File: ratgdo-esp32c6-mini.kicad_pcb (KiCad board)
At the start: 2 copper layers, 29 parts, among them J1 USB_C_Receptacle_USB2.0_14P, J2 Screw_Terminal_01x03, Q1 2N7002, Q2 AO3400A, SW1 RESET, SW2 BOOTSEL, U1 USBLC6-2SC6, U2 ESP32-C6-MINI-1/U, U3 RS3236-3.3YF5

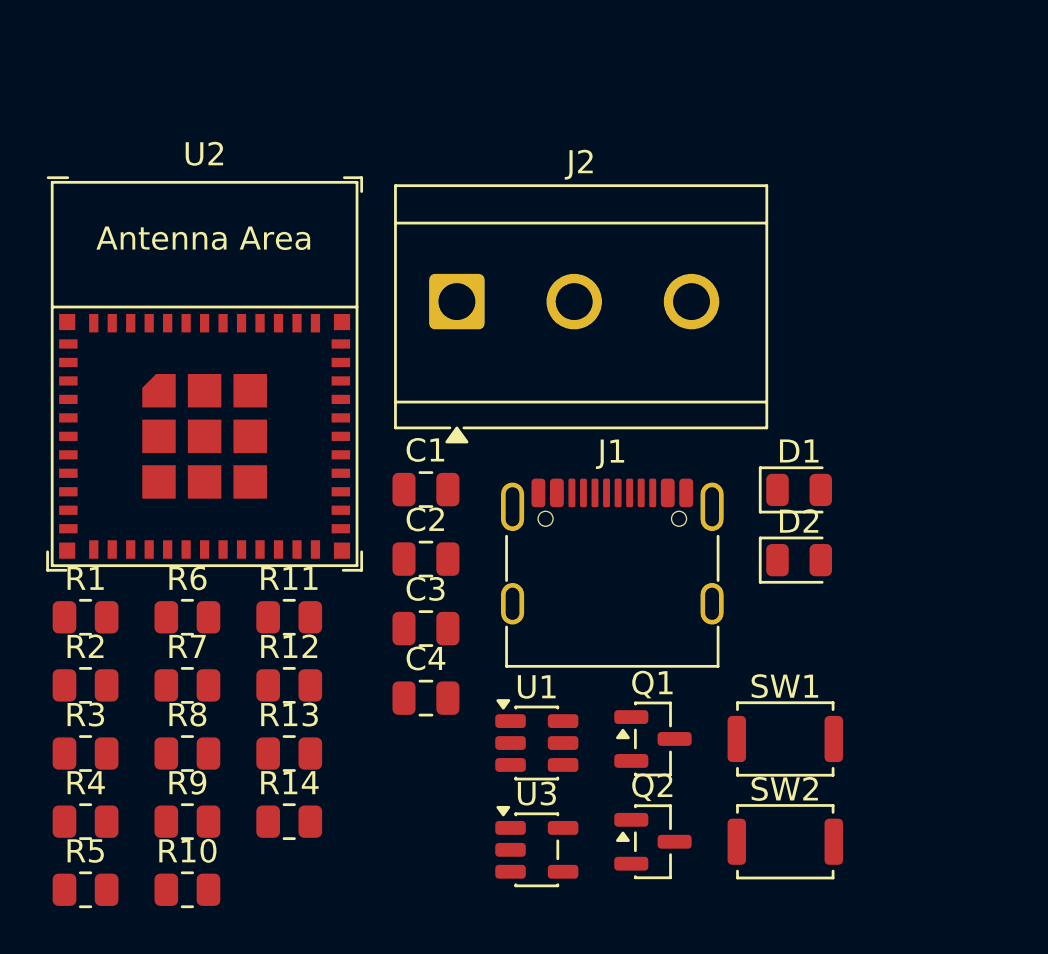
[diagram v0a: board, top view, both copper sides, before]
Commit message: change R&C to 0402 size
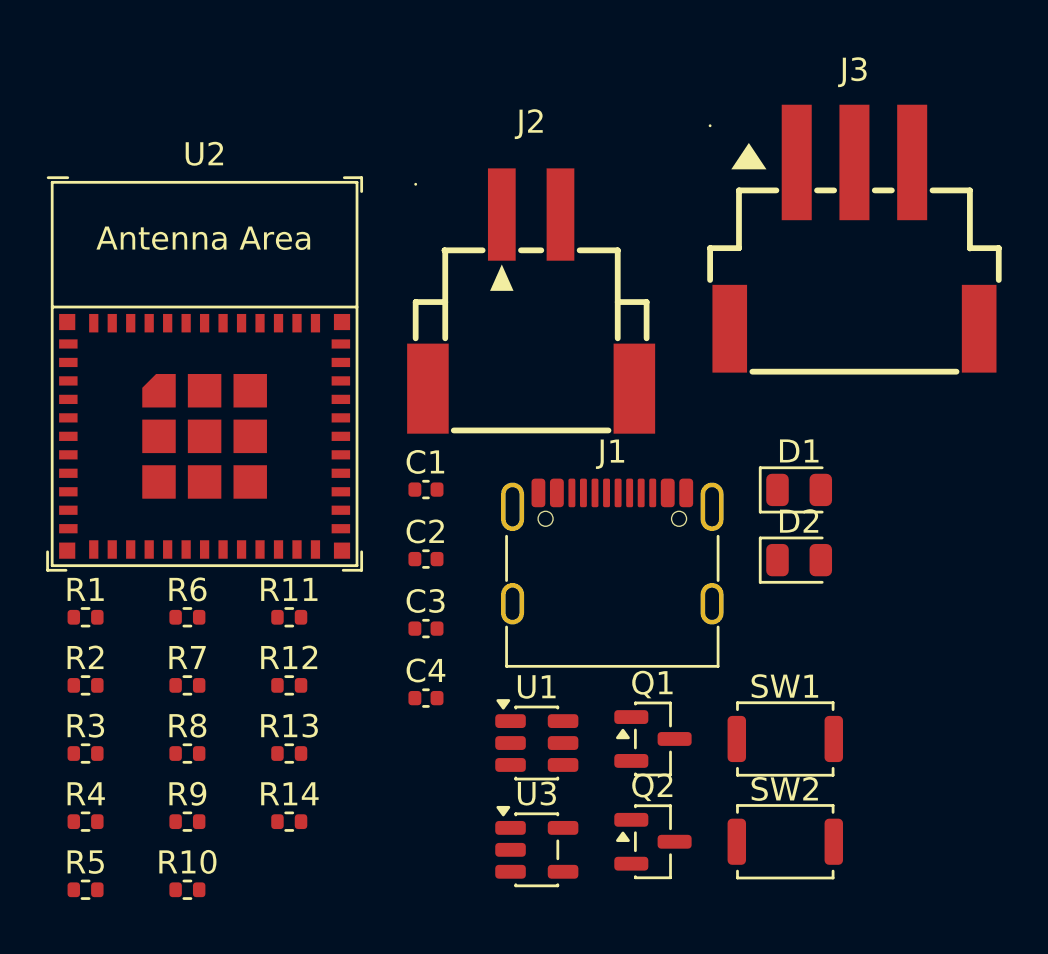
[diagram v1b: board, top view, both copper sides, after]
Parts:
- added J3: Conn_01x03, LCSC:CONN-SMD_3P-P2.50_HX-2.54-3P-WT, F.Cu at (63.5, 29.0)
- C1, C2, C3, C4: footprint Capacitor_SMD:C_0805_2012Metric -> Capacitor_SMD:C_0402_1005Metric
- J2: value Screw_Terminal_01x03 -> Conn_01x02; footprint TerminalBlock_CUI:TerminalBlock_CUI_TB007-508-03_1x03_P5.08mm_Horizontal -> LCSC:CONN-SMD_2P-P2.54-XH2.54-WT
- R1, R10, R11, R12, R13, R14, R2, R3, R4, R5, R6, R7, R8, R9: footprint Resistor_SMD:R_0805_2012Metric -> Resistor_SMD:R_0402_1005Metric
- moved J2 3.22 mm to (49.5, 31.4)
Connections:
- J2 pad 1: BLK/OBST -> +5V
- J2 pad 2: RED/CTRL -> GND
- J2 pad 3: GND -> (no net)

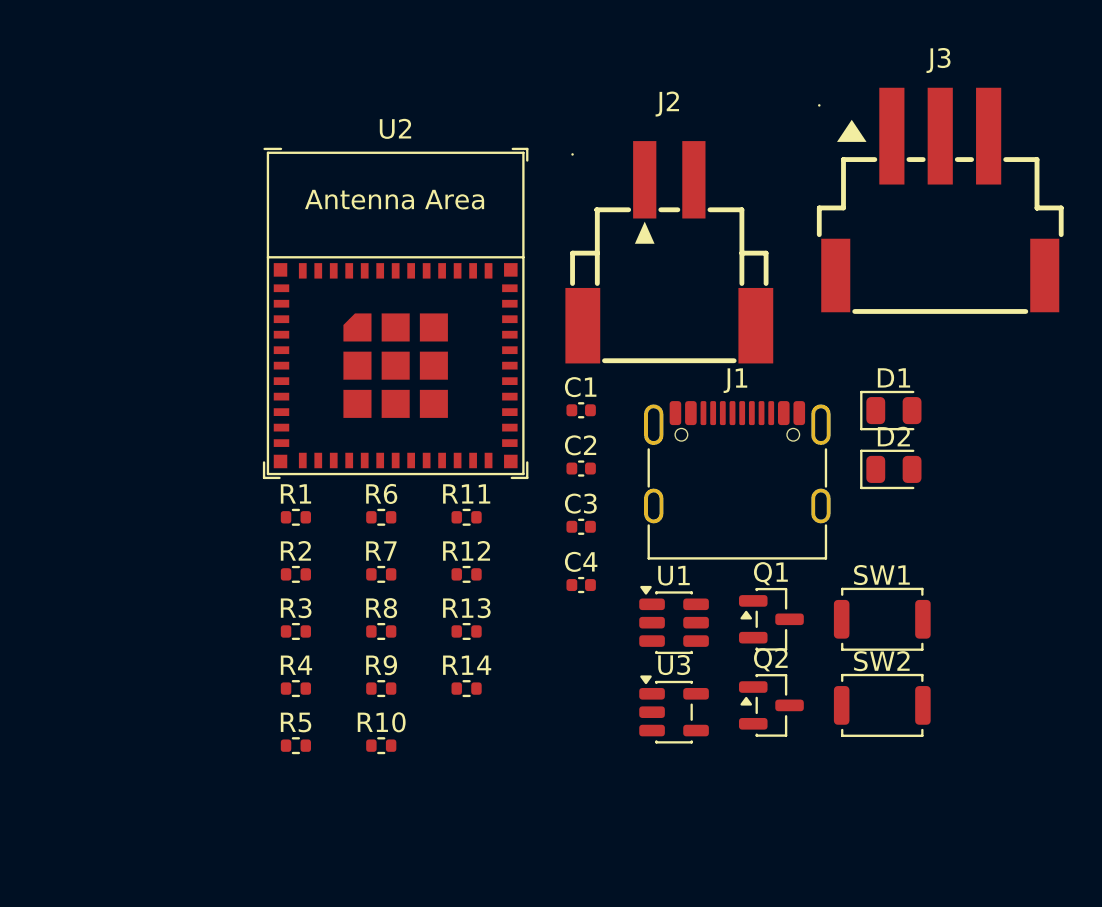
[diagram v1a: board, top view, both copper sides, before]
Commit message: sync pcb with schematic
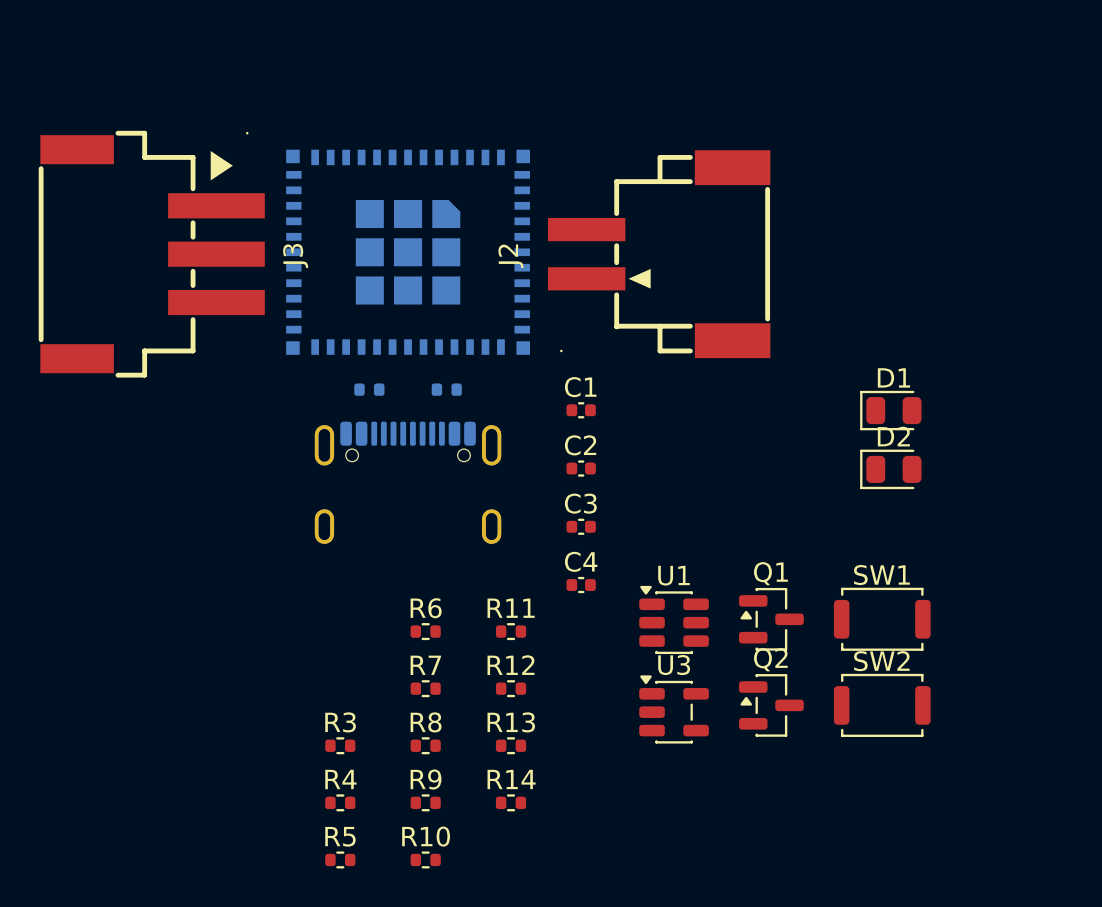
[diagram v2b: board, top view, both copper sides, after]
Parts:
- J1, R1, R2, U2: moved to B.Cu
- moved J3 41.1 mm to (22.5, 31.5), turned to -90 degrees
- moved J1 17.0 mm to (36.0, 44.5), turned to 180 degrees
- moved R2 10.3 mm to (34.0, 38.5), turned to 180 degrees
- moved R1 10.2 mm to (38.0, 38.5)
- moved R11 6.34 mm to (41.3, 51.0)
- moved R12 6.34 mm to (41.3, 54.0)
- moved R13 6.34 mm to (41.3, 56.9)
- moved R14 6.34 mm to (41.3, 59.9)
- moved R3 6.34 mm to (32.5, 56.9)
- moved R4 6.34 mm to (32.5, 59.9)
- moved R6 6.34 mm to (36.9, 51.0)
- moved R7 6.34 mm to (36.9, 54.0)
- moved R8 6.34 mm to (36.9, 56.9)
- moved R9 6.34 mm to (36.9, 59.9)
- moved R5 6.34 mm to (32.5, 62.8)
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
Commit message: layout components
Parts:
- J1: value USB_C_Receptacle_USB2.0_14P -> USB_C_2.0
- J2, J3: moved to B.Cu
- R1, R2: moved to F.Cu
- U2: value ESP32-C6-MINI-1/U -> ESP32-C6-MINI
- U3: value RS3236-3.3YF5 -> RS3236
- moved R1 139.8 mm to (161.0, 105.0)
- moved J2 139.4 mm to (171.0, 99.0), turned to -90 degrees
- moved J3 139.3 mm to (144.5, 98.8), turned to 90 degrees
- moved U2 138.3 mm to (158.0, 93.9)
- moved R2 138.1 mm to (155.0, 105.0)
- moved J1 137.9 mm to (158.0, 108.7)
- moved C1 135.1 mm to (166.0, 99.5), turned to -90 degrees
- moved R3 133.8 mm to (159.0, 100.5)
- moved R4 131.0 mm to (157.0, 100.5), turned to 180 degrees
- moved R14 129.2 mm to (164.0, 100.5), turned to 180 degrees
- moved R9 128.9 mm to (160.5, 96.5), turned to -90 degrees
- moved C2 128.9 mm to (162.5, 95.5), turned to 180 degrees
- moved C3 128.5 mm to (162.5, 97.5), turned to 180 degrees
- moved C4 128.0 mm to (162.0, 100.5), turned to 180 degrees
- moved R5 126.5 mm to (153.6, 99.5), turned to 90 degrees
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
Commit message: wiring
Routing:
- net +5V: track 0.00 -> 25.4 mm, vias 0 -> 3
- net SENSOR: track 0.00 -> 20.8 mm, vias 0 -> 1
- net +3V3: track 0.00 -> 15.5 mm
- net /ENABLE: track 0.00 -> 11.7 mm, vias 0 -> 2
- net /BOOTSEL: track 0.00 -> 9.45 mm, vias 0 -> 1
- net RED/CTRL: track 0.00 -> 7.53 mm, vias 0 -> 1
- net /STATUS_LED: track 0.00 -> 6.95 mm, vias 0 -> 1
- net SERIAL_TX: track 0.00 -> 3.82 mm, vias 0 -> 1
- net BLK/OBST: track 0.00 -> 3.65 mm, vias 0 -> 1
- net Net-(J1-CC1): track 0.00 -> 2.89 mm, vias 0 -> 1
- net Net-(J1-D--PadA7): track 0.00 -> 2.83 mm, vias 0 -> 1
- net Net-(J1-D+-PadA6): track 0.00 -> 2.82 mm, vias 0 -> 1
- net Net-(J1-CC2): track 0.00 -> 2.43 mm, vias 0 -> 1
- net SERIAL_RX: track 0.00 -> 2.36 mm, vias 0 -> 1
- net Net-(U2-GPIO12/USB_D-): track 0.00 -> 2.14 mm, vias 0 -> 1
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
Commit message: edge
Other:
- board outline added: 37.5 x 27.5 mm
- board text added: "BOOT"
- board text added: "PWR"
- board text added: "RESET"
- board text added: "STAT"

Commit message: wiring & cut
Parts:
- U3: value RS3236 -> RS3236-3.3YF5
- moved R3 0.50 mm to (159.5, 100.5), turned to -90 degrees
- moved R4 0.50 mm to (156.5, 100.5), turned to -90 degrees
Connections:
- J2 pad 3: (no net) -> GND
- J2 pad 4: (no net) -> GND
- J3 pad 4: (no net) -> GND
- J3 pad 5: (no net) -> GND
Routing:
- net GND: track 0.00 -> 133.4 mm, vias 0 -> 7
- net +3V3: track 15.5 -> 20.3 mm, vias 0 -> 1
- net Net-(J1-D--PadA7): track 2.83 -> 5.50 mm
- net Net-(J1-D+-PadA6): track 2.82 -> 4.81 mm
- net Net-(U2-GPIO13/USB_D+): track 1.21 -> 2.56 mm
- net Net-(U2-GPIO12/USB_D-): track 2.14 -> 3.34 mm
- net /ENABLE: track 11.7 -> 10.6 mm
- net USB_D-: track 2.09 -> 1.58 mm
- net USB_D+: track 2.09 -> 1.58 mm
- added copper zone on B.Cu, net GND
- added copper zone on F.Cu, net GND
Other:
- board size 37.5 x 27.5 mm -> 38.8 x 27.5 mm

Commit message: add wire label
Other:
- board text added: "5V"
- board text added: "CTRL(R)"
- board text added: "GND"
- board text added: "GND(W)"
- board text added: "OBST(B)"
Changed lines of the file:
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@@
+		)
+	)
+	(gr_text " 5V"
+		(at 168.78 96.9 0)
+		(layer "B.SilkS")
+		(effects
+			(font
+				(size 0.6 0.6)
+				(thickness 0.1)
+			)
+			(justify left bottom mirror)
+		)
+	)
+	(gr_text " GND"
+		(at 168.78 99.44 0)
+		(layer "B.SilkS")
+		(effects
+			(font
+				(size 0.6 0.6)
+				(thickness 0.1)
+			)
+			(justify left bottom mirror)
+		)
+	)
+	(gr_text "GND(W) "
+		(at 146.89 95.37 0)
+		(layer "B.SilkS")
+		(effects
+			(font
+				(size 0.6 0.6)
+				(thickness 0.1)
+			)
+			(justify right bottom mirror)
+		)
+	)
+	(gr_text "CTRL(R) "
+		(at 146.89 97.87 0)
+		(layer "B.SilkS")
+		(effects
+			(font
+				(size 0.6 0.6)
+				(thickness 0.1)
+			)
+			(justify right bottom mirror)
+		)
+	)
+	(gr_text "OBST(B) "
+		(at 146.89 100.37 0)
+		(layer "B.SilkS")
+		(effects
+			(font
+				(size 0.6 0.6)
+				(thickness 0.1)
+			)
+			(justify right bottom mirror)
 		)
 	)
